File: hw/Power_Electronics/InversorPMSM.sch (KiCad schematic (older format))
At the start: 4 parts

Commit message: advances were made on power electronics board
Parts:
- removed Q?: IRF3205, Package_TO_SOT_THT:TO-220-3_Vertical, symbol Transistor_FET:IRF3205
- added C1, C2, C3, C4, C5, C6: 33pF, Capacitor_SMD:C_0603_1608Metric, symbol Device:C
- added C10, C11, C12: 470nF, Capacitor_SMD:C_0603_1608Metric, symbol Device:C
- added C13, C14, C15, C16, C17, C18, C9: DNM, Capacitor_SMD:C_0603_1608Metric, symbol Device:C
- added C7, C8: 100nF, Capacitor_SMD:C_0603_1608Metric, symbol Device:C
- added D1, D10, D6, D7, D8, D9: B5819W, inversor-pmsm:D_SOD-123, symbol Device:D_Schottky
- added D2, D3, D4: DNM, inversor-pmsm:D_SOD-123, symbol Device:D_Schottky
- added J1: FROM_CONTROL_BOARD, Connector_IDC:IDC-Header_2x13_P2.54mm_Vertical, symbol Connector_Generic:Conn_02x13_Odd_Even
- added Q1, Q2, Q3, Q4, Q5, Q6: HY1908D, inversor-pmsm:Universal_MOSFET_generic, symbol Transistor_FET:IRF3205
- added Q10, Q11, Q12, Q7, Q8, Q9: JCS24N50WH, symbol Transistor_FET:IRF3205
- added R1, R2, R3, R4, R5, R6: 1K, Resistor_SMD:R_0603_1608Metric, symbol Device:R
- added R10: 5.6K, Resistor_SMD:R_0805_2012Metric, symbol Device:R
- added R11, R12, R13: 27R, Resistor_SMD:R_0603_1608Metric, symbol Device:R
- added R15, R16, R17, R18, R19: 10R, Resistor_SMD:R_0603_1608Metric, symbol Device:R
- added R21, R22, R23, R24, R25: 100R, Resistor_SMD:R_0603_1608Metric, symbol Device:R
- added R26, R27, R28, R29, R30, R31, R7: 100K, Resistor_SMD:R_0603_1608Metric, symbol Device:R
- added R8, R9: 100K, Resistor_SMD:R_0805_2012Metric, symbol Device:R
- added TP1, TP10, TP11, TP12, TP13, TP14, TP15, TP16, TP17, TP18, TP19, TP2, TP20, TP21, TP22, TP23, TP24, TP28, TP29, TP3, TP30, TP4, TP5, TP6, TP7, TP8, TP9: TestPoint, TestPoint:TestPoint_Pad_D1.5mm, symbol Connector:TestPoint
- added U1: STDRIVE601, Package_SO:SOIC-28W_7.5x17.9mm_P1.27mm, symbol inversor-pmsm:STDRIVE601
- D5: renamed from D?; footprint Diode_SMD:D_SOD-123 -> inversor-pmsm:D_SOD-123
- gave numbers to parts that had none: 2
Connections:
- net at R14.1: now also D5.1 (K)
- net at R14.2: now also R20.2, TP6.1, U1.27 (HVG1)
- net GH1: now reaches R20.1
- net GH1: now also D5.2 (A), C13.2, Q1.1 (G), Q7.1 (G), R26.1, TP13.1
- new net: D6.1 (K), R15.1
- new net: R15.2, R21.2, TP8.1, U1.16 (LVG1)
- new net: D7.1 (K), R16.1
- new net: R16.2, R22.2, TP4.1, U1.23 (HVG2)
- new net: D8.1 (K), R17.1
- new net: R17.2, R23.2, TP12.1, U1.15 (LVG2)
- new net: D9.1 (K), R18.1
- new net: R18.2, R24.2, TP11.1, U1.19 (HVG3)
- new net: D10.1 (K), R19.1
- new net: R19.2, R25.2, TP9.1, U1.14 (LVG3)
- new net: J1.16 (Pin_16), R6.2
- new net: J1.14 (Pin_14), R5.2
- new net: J1.12 (Pin_12), R4.2
- new net: J1.10 (Pin_10), R3.2
- new net: J1.8 (Pin_8), R2.2
- new net: J1.6 (Pin_6), R1.2
- new net: R8.2, R9.2
- new net: D2.2 (A), R11.1
- new net: D3.2 (A), R12.1
- new net: D4.2 (A), R13.1
- new net: C7.1, R7.2, TP1.1, U1.11 (OD)
- new net +12V: J1.23 (Pin_23), J1.24 (Pin_24), J1.3 (Pin_3), J1.4 (Pin_4), R7.1, TP2.1, U1.1 (VCC)
- new net +3V3: D1.1 (K)
- new net +5V: J1.21 (Pin_21)
- new net BOOT1: C10.1, D2.1 (K), U1.28 (BOOT1)
- new net BOOT2: C11.1, D3.1 (K), U1.24 (BOOT2)
- new net BOOT3: C12.1, D4.1 (K), U1.20 (BOOT3)
- new net CIN: U1.9 (CIN)
- new net ENABLE: J1.20 (Pin_20), U1.10 (EN)
- new net GH2: C15.2, D7.2 (A), Q3.1 (G), Q9.1 (G), R22.1, R28.1, TP15.1
- new net GH3: C17.2, D9.2 (A), Q11.1 (G), Q5.1 (G), R24.1, R30.1, TP17.1
- new net GL1: C14.2, D6.2 (A), Q2.1 (G), Q8.1 (G), R21.1, R27.1, TP14.1
- new net GL2: C16.2, D8.2 (A), Q10.1 (G), Q4.1 (G), R23.1, R29.1, TP16.1
- new net GL3: C18.2, D10.2 (A), Q12.1 (G), Q6.1 (G), R25.1, R31.1, TP18.1
- new net GND: C1.2, C2.2, C3.2, C4.2, C5.2, C6.2, C7.2, C8.2, C9.2, J1.1 (Pin_1), J1.2 (Pin_2), J1.25 (Pin_25), J1.26 (Pin_26), R10.2, TP28.1, TP29.1, TP30.1, U1.12 (SGND), U1.13 (PGND)
- new net HALL1: J1.19 (Pin_19)
- new net HALL2: J1.17 (Pin_17)
- new net HALL3: J1.15 (Pin_15)
- new net HV: Q1.2 (D), Q11.2 (D), Q3.2 (D), Q5.2 (D), Q7.2 (D), Q9.2 (D), R8.1
- new net OUT1: C10.2, C13.1, Q1.3 (S), Q2.2 (D), Q7.3 (S), Q8.2 (D), R26.2, TP19.1, TP7.1, U1.26 (OUT1)
- new net OUT2: C11.2, C15.1, Q10.2 (D), Q3.3 (S), Q4.2 (D), Q9.3 (S), R28.2, TP21.1, TP5.1, U1.22 (OUT2)
- new net OUT3: C12.2, C17.1, Q11.3 (S), Q12.2 (D), Q5.3 (S), Q6.2 (D), R30.2, TP10.1, TP23.1, U1.18 (OUT3)
- new net SENSE1: C14.1, Q2.3 (S), Q8.3 (S), R27.2, TP20.1
- new net SENSE2: C16.1, Q10.3 (S), Q4.3 (S), R29.2, TP22.1
- new net SENSE3: C18.1, Q12.3 (S), Q6.3 (S), R31.2, TP24.1
- new net SENSE_OUT1: J1.9 (Pin_9)
- new net SENSE_OUT2: J1.11 (Pin_11)
- new net SENSE_OUT3: J1.13 (Pin_13)
- new net U_H: C1.1, R1.1, U1.2 (~HIN1)
- new net U_L: C4.1, R4.1, U1.5 (~LIN1)
- new net VBUS_SCALED: C8.1, C9.1, D1.2 (A), J1.22 (Pin_22), R10.1, R9.1, TP3.1
- new net VCC: R11.2, R12.2, R13.2
- new net V_H: C2.1, R2.1, U1.3 (~HIN2)
- new net V_L: C5.1, R5.1, U1.6 (~LIN2)
- new net W_H: C3.1, R3.1, U1.4 (~HIN3)
- new net W_L: C6.1, R6.1, U1.7 (~LIN3)
- new net ~ERROR: J1.18 (Pin_18), U1.8 (~FAULT)
- no-connect marks 0 -> 2
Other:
- note added: "110V≡3V"
- note added: "RESERVED"
- moved on the sheet: D5, R14, R20

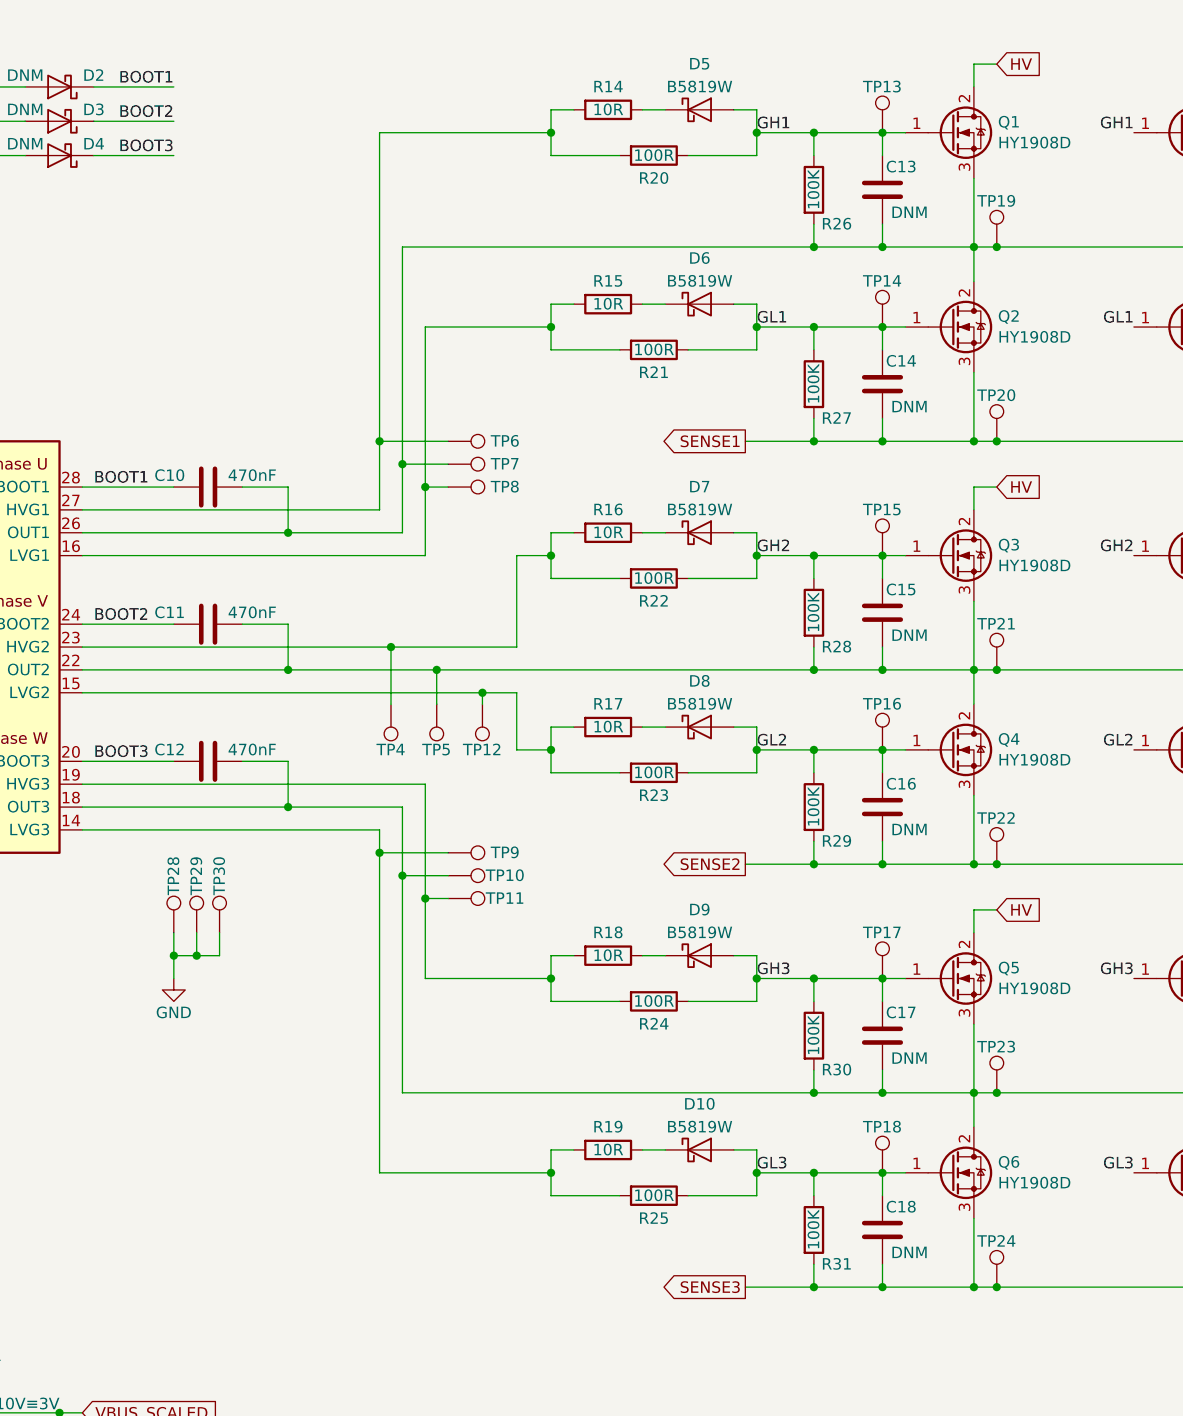
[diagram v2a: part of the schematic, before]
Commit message: all component's positions are more or less defined
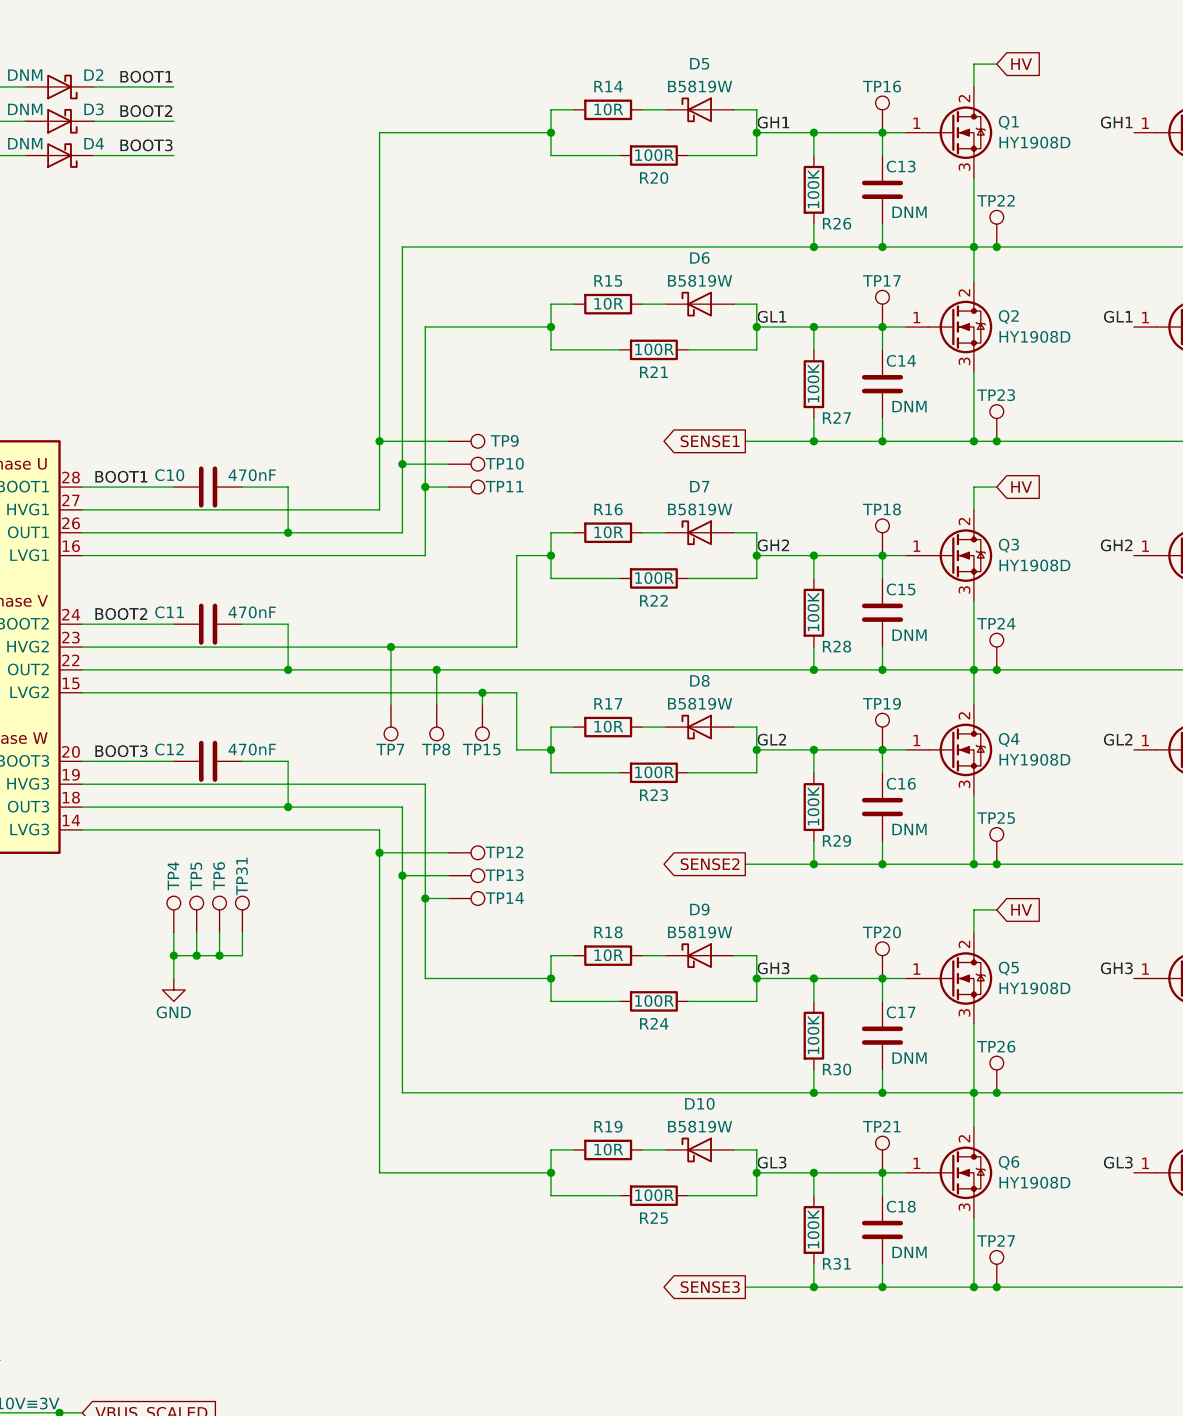
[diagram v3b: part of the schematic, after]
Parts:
- added TP31: TestPoint, TestPoint:TestPoint_Pad_D1.5mm, symbol Connector:TestPoint
- renumbered TP7 to TP10, TP8 to TP11, TP9 to TP12, TP10 to TP13, TP11 to TP14, TP12 to TP15, TP13 to TP16, TP14 to TP17, TP15 to TP18, TP16 to TP19, TP17 to TP20, TP18 to TP21, TP19 to TP22, TP20 to TP23, TP21 to TP24, TP22 to TP25, TP23 to TP26, TP24 to TP27, TP28 to TP4, TP29 to TP5, TP30 to TP6, TP4 to TP7, TP5 to TP8, TP6 to TP9
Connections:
- net GND: now also TP31.1
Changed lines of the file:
@@
 GH1
 $Comp
-L Connector:TestPoint TP13
+L Connector:TestPoint TP16
 U 1 1 5FC1A478
 P 9100 1300
-F 0 "TP13" H 9100 1500 50  0000 C CNN
+F 0 "TP16" H 9100 1500 50  0000 C CNN
 F 1 "TestPoint" H 9158 1327 50  0001 L CNN
 F 2 "TestPoint:TestPoint_Pad_D1.5mm" H 9300 1300 50  0001 C CNN
@@
 	9100 2150 8800 2150
 $Comp
-L Connector:TestPoint TP14
+L Connector:TestPoint TP17
 U 1 1 5FC2D27B
 P 9100 2150
-F 0 "TP14" H 9100 2350 50  0000 C CNN
+F 0 "TP17" H 9100 2350 50  0000 C CNN
 F 1 "TestPoint" H 9158 2177 50  0001 L CNN
 F 2 "TestPoint:TestPoint_Pad_D1.5mm" H 9300 2150 50  0001 C CNN
@@
 Connection ~ 8800 1300
 $Comp
-L Connector:TestPoint TP19
+L Connector:TestPoint TP22
 U 1 1 5FC3D5A8
 P 9600 1800
-F 0 "TP19" H 9600 2000 50  0000 C CNN
+F 0 "TP22" H 9600 2000 50  0000 C CNN
 F 1 "TestPoint" H 9658 1827 50  0001 L CNN
 F 2 "TestPoint:TestPoint_Pad_D1.5mm" H 9800 1800 50  0001 C CNN
@@
 	8550 2150 8550 2250
 $Comp
-L Connector:TestPoint TP20
+L Connector:TestPoint TP23
 U 1 1 5FC4D2ED
 P 9600 2650
-F 0 "TP20" H 9600 2850 50  0000 C CNN
+F 0 "TP23" H 9600 2850 50  0000 C CNN
 F 1 "TestPoint" H 9658 2677 50  0001 L CNN
 F 2 "TestPoint:TestPoint_Pad_D1.5mm" H 9800 2650 50  0001 C CNN
@@
 GH2
 $Comp
-L Connector:TestPoint TP15
+L Connector:TestPoint TP18
 U 1 1 5FC63C93
 P 9100 3150
-F 0 "TP15" H 9100 3350 50  0000 C CNN
+F 0 "TP18" H 9100 3350 50  0000 C CNN
 F 1 "TestPoint" H 9158 3177 50  0001 L CNN
 F 2 "TestPoint:TestPoint_Pad_D1.5mm" H 9300 3150 50  0001 C CNN
@@
 	9100 4000 8800 4000
 $Comp
-L Connector:TestPoint TP16
+L Connector:TestPoint TP19
 U 1 1 5FC63CA8
 P 9100 4000
-F 0 "TP16" H 9100 4200 50  0000 C CNN
+F 0 "TP19" H 9100 4200 50  0000 C CNN
 F 1 "TestPoint" H 9158 4027 50  0001 L CNN
 F 2 "TestPoint:TestPoint_Pad_D1.5mm" H 9300 4000 50  0001 C CNN
@@
 Connection ~ 8800 3150
 $Comp
-L Connector:TestPoint TP21
+L Connector:TestPoint TP24
 U 1 1 5FC63CD4
 P 9600 3650
-F 0 "TP21" H 9600 3850 50  0000 C CNN
+F 0 "TP24" H 9600 3850 50  0000 C CNN
 F 1 "TestPoint" H 9658 3677 50  0001 L CNN
 F 2 "TestPoint:TestPoint_Pad_D1.5mm" H 9800 3650 50  0001 C CNN
@@
 	8550 4000 8550 4100
 $Comp
-L Connector:TestPoint TP22
+L Connector:TestPoint TP25
 U 1 1 5FC63D09
 P 9600 4500
-F 0 "TP22" H 9600 4700 50  0000 C CNN
+F 0 "TP25" H 9600 4700 50  0000 C CNN
 F 1 "TestPoint" H 9658 4527 50  0001 L CNN
 F 2 "TestPoint:TestPoint_Pad_D1.5mm" H 9800 4500 50  0001 C CNN
@@
 GH3
 $Comp
-L Connector:TestPoint TP17
+L Connector:TestPoint TP20
 U 1 1 5FC851E9
 P 9100 5000
-F 0 "TP17" H 9100 5200 50  0000 C CNN
+F 0 "TP20" H 9100 5200 50  0000 C CNN
 F 1 "TestPoint" H 9158 5027 50  0001 L CNN
 F 2 "TestPoint:TestPoint_Pad_D1.5mm" H 9300 5000 50  0001 C CNN
@@
 	9100 5850 8800 5850
 $Comp
-L Connector:TestPoint TP18
+L Connector:TestPoint TP21
 U 1 1 5FC851FE
 P 9100 5850
-F 0 "TP18" H 9100 6050 50  0000 C CNN
+F 0 "TP21" H 9100 6050 50  0000 C CNN
 F 1 "TestPoint" H 9158 5877 50  0001 L CNN
 F 2 "TestPoint:TestPoint_Pad_D1.5mm" H 9300 5850 50  0001 C CNN
@@
 Connection ~ 8800 5000
 $Comp
-L Connector:TestPoint TP23
+L Connector:TestPoint TP26
 U 1 1 5FC8522A
 P 9600 5500
-F 0 "TP23" H 9600 5700 50  0000 C CNN
+F 0 "TP26" H 9600 5700 50  0000 C CNN
 F 1 "TestPoint" H 9658 5527 50  0001 L CNN
 F 2 "TestPoint:TestPoint_Pad_D1.5mm" H 9800 5500 50  0001 C CNN
@@
 	8550 5850 8550 5950
 $Comp
-L Connector:TestPoint TP24
+L Connector:TestPoint TP27
 U 1 1 5FC8525F
 P 9600 6350
-F 0 "TP24" H 9600 6550 50  0000 C CNN
+F 0 "TP27" H 9600 6550 50  0000 C CNN
 F 1 "TestPoint" H 9658 6377 50  0001 L CNN
 F 2 "TestPoint:TestPoint_Pad_D1.5mm" H 9800 6350 50  0001 C CNN
@@
 	6900 2650 6900 2950
 $Comp
-L Connector:TestPoint TP8
+L Connector:TestPoint TP11
 U 1 1 5FDC690E
 P 7200 2850
-F 0 "TP8" V 7200 3100 50  0000 C CNN
+F 0 "TP11" V 7200 3100 50  0000 C CNN
 F 1 "TestPoint" H 7258 2877 50  0001 L CNN
 F 2 "TestPoint:TestPoint_Pad_D1.5mm" H 7400 2850 50  0001 C CNN
@@
 $EndComp
 $Comp
-L Connector:TestPoint TP7
+L Connector:TestPoint TP10
 U 1 1 5FE036EF
 P 7200 2750
-F 0 "TP7" V 7200 3000 50  0000 C CNN
+F 0 "TP10" V 7200 3000 50  0000 C CNN
 F 1 "TestPoint" H 7258 2777 50  0001 L CNN
 F 2 "TestPoint:TestPoint_Pad_D1.5mm" H 7400 2750 50  0001 C CNN
@@
 $EndComp
 $Comp
-L Connector:TestPoint TP6
+L Connector:TestPoint TP9
 U 1 1 5FDFA4B3
 P 7200 2650
-F 0 "TP6" V 7200 2900 50  0000 C CNN
+F 0 "TP9" V 7200 2900 50  0000 C CNN
 F 1 "TestPoint" H 7258 2677 50  0001 L CNN
 F 2 "TestPoint:TestPoint_Pad_D1.5mm" H 7400 2650 50  0001 C CNN
@@
 $EndComp
 $Comp
-L Connector:TestPoint TP11
+L Connector:TestPoint TP14
 U 1 1 5FE9EDA3
 P 7200 4650
-F 0 "TP11" V 7200 4900 50  0000 C CNN
+F 0 "TP14" V 7200 4900 50  0000 C CNN
 F 1 "TestPoint" H 7258 4677 50  0001 L CNN
 F 2 "TestPoint:TestPoint_Pad_D1.5mm" H 7400 4650 50  0001 C CNN
@@
 $EndComp
 $Comp
-L Connector:TestPoint TP10
+L Connector:TestPoint TP13
 U 1 1 5FE9EDAD
 P 7200 4550
-F 0 "TP10" V 7200 4800 50  0000 C CNN
+F 0 "TP13" V 7200 4800 50  0000 C CNN
 F 1 "TestPoint" H 7258 4577 50  0001 L CNN
 F 2 "TestPoint:TestPoint_Pad_D1.5mm" H 7400 4550 50  0001 C CNN
@@
 $EndComp
 $Comp
-L Connector:TestPoint TP9
+L Connector:TestPoint TP12
 U 1 1 5FE9EDB7
 P 7200 4450
-F 0 "TP9" V 7200 4700 50  0000 C CNN
+F 0 "TP12" V 7200 4700 50  0000 C CNN
 F 1 "TestPoint" H 7258 4477 50  0001 L CNN
 F 2 "TestPoint:TestPoint_Pad_D1.5mm" H 7400 4450 50  0001 C CNN
@@
 	7100 4650 7100 5000
 $Comp
-L Connector:TestPoint TP4
+L Connector:TestPoint TP7
 U 1 1 5FEC84E5
 P 6950 3800
-F 0 "TP4" H 6950 4000 50  0000 C CNN
+F 0 "TP7" H 6950 4000 50  0000 C CNN
 F 1 "TestPoint" H 7008 3827 50  0001 L CNN
 F 2 "TestPoint:TestPoint_Pad_D1.5mm" H 7150 3800 50  0001 C CNN
@@
 $EndComp
 $Comp
-L Connector:TestPoint TP5
+L Connector:TestPoint TP8
 U 1 1 5FEC84EF
 P 7150 3800
-F 0 "TP5" H 7150 4000 50  0000 C CNN
+F 0 "TP8" H 7150 4000 50  0000 C CNN
 F 1 "TestPoint" H 7208 3827 50  0001 L CNN
 F 2 "TestPoint:TestPoint_Pad_D1.5mm" H 7350 3800 50  0001 C CNN
@@
 $EndComp
 $Comp
-L Connector:TestPoint TP12
+L Connector:TestPoint TP15
 U 1 1 5FEC84F9
 P 7350 3800
-F 0 "TP12" H 7350 4000 50  0000 C CNN
+F 0 "TP15" H 7350 4000 50  0000 C CNN
 F 1 "TestPoint" H 7408 3827 50  0001 L CNN
 F 2 "TestPoint:TestPoint_Pad_D1.5mm" H 7550 3800 50  0001 C CNN
@@
 $EndComp
 $Comp
-L Connector:TestPoint TP28
+L Connector:TestPoint TP4
 U 1 1 60E5047E
 P 6000 4800
-F 0 "TP28" V 6000 5050 50  0000 C CNN
+F 0 "TP4" V 6000 5050 50  0000 C CNN
 F 1 "TestPoint" H 6058 4827 50  0001 L CNN
 F 2 "TestPoint:TestPoint_Pad_D1.5mm" H 6200 4800 50  0001 C CNN
@@
 $EndComp
 $Comp
-L power:GND #PWR0101
+L power:GND #PWR025
 U 1 1 60E51D1A
 P 6000 5000
-F 0 "#PWR0101" H 6000 4750 50  0001 C CNN
+F 0 "#PWR025" H 6000 4750 50  0001 C CNN
 F 1 "GND" H 6000 4850 50  0000 C CNN
 F 2 "" H 6000 5000 50  0001 C CNN
@@
 	6000 5000 6000 4900
 $Comp
-L Connector:TestPoint TP29
+L Connector:TestPoint TP5
 U 1 1 60E87EBE
 P 6100 4800
-F 0 "TP29" V 6100 5050 50  0000 C CNN
+F 0 "TP5" V 6100 5050 50  0000 C CNN
 F 1 "TestPoint" H 6158 4827 50  0001 L CNN
 F 2 "TestPoint:TestPoint_Pad_D1.5mm" H 6300 4800 50  0001 C CNN
@@
 $EndComp
 $Comp
-L Connector:TestPoint TP30
+L Connector:TestPoint TP6
 U 1 1 60E8805F
 P 6200 4800
-F 0 "TP30" V 6200 5050 50  0000 C CNN
+F 0 "TP6" V 6200 5050 50  0000 C CNN
 F 1 "TestPoint" H 6258 4827 50  0001 L CNN
 F 2 "TestPoint:TestPoint_Pad_D1.5mm" H 6400 4800 50  0001 C CNN
@@
 Text GLabel 1050 6900 0    50   Input ~ 0
 HALL3
+$Comp
+L Connector:TestPoint TP31
+U 1 1 600B6978
+P 6300 4800
+F 0 "TP31" V 6300 5050 50  0000 C CNN
+F 1 "TestPoint" H 6358 4827 50  0001 L CNN
+F 2 "TestPoint:TestPoint_Pad_D1.5mm" H 6500 4800 50  0001 C CNN
+F 3 "~" H 6500 4800 50  0001 C CNN
+	1    6300 4800
+	1    0    0    -1
+$EndComp
+Wire Wire Line
+	6300 4800 6300 4900
+Wire Wire Line
+	6300 4900 6200 4900
+Connection ~ 6200 4900
 $EndSCHEMATC
